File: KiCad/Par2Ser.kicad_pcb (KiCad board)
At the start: 2 copper layers, 47 x 50 mm, 42 parts, among them J1 DB25_Male, J2 Arduino UART header, J3 USB_C_Receptacle_USB2.0, J4 Conn_01x02, Q1 BC857, U1 Arduino_Nano_V3, U2 FT232RNL-REEL, U3 SC16IS750IBS,128, X1 Abracon-ASFL1-7.3728MHZ-EK-T

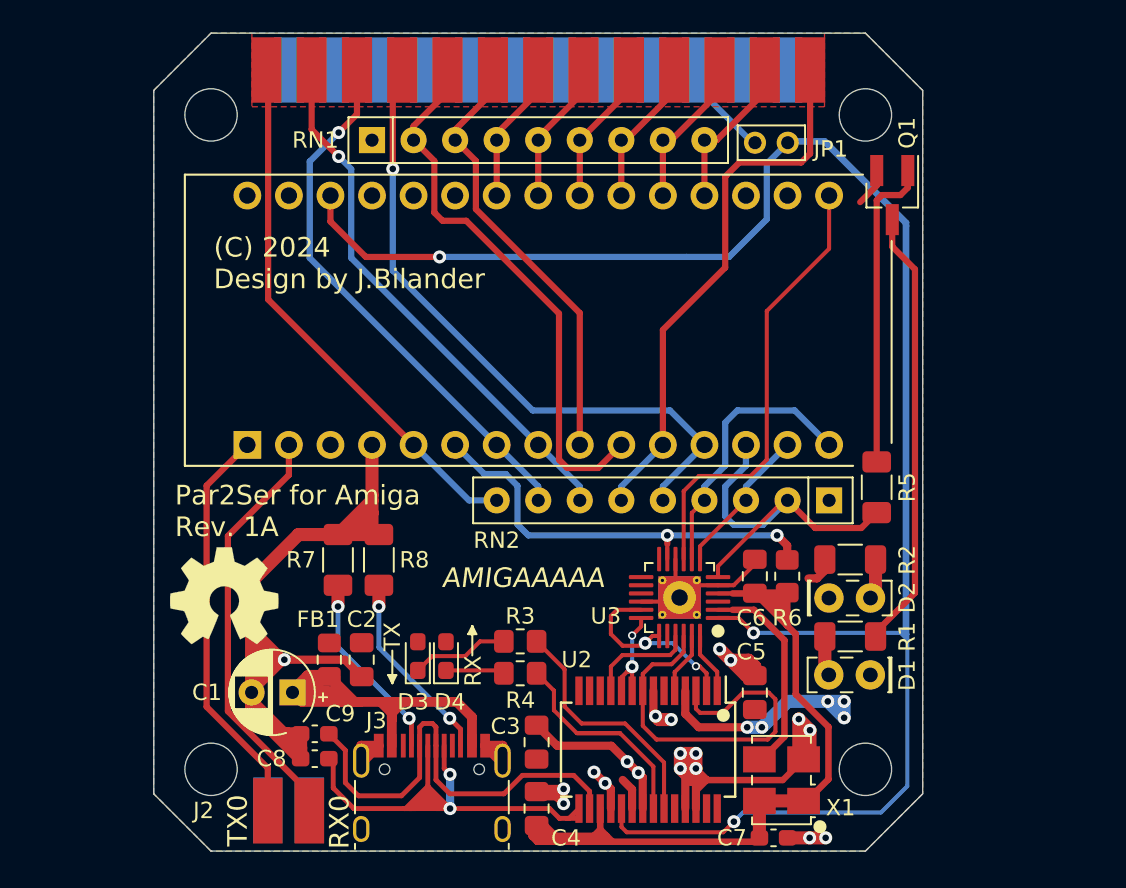
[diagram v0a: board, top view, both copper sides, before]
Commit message: Add LC4032V-5TN48C CPLD and remove Arduino Nano
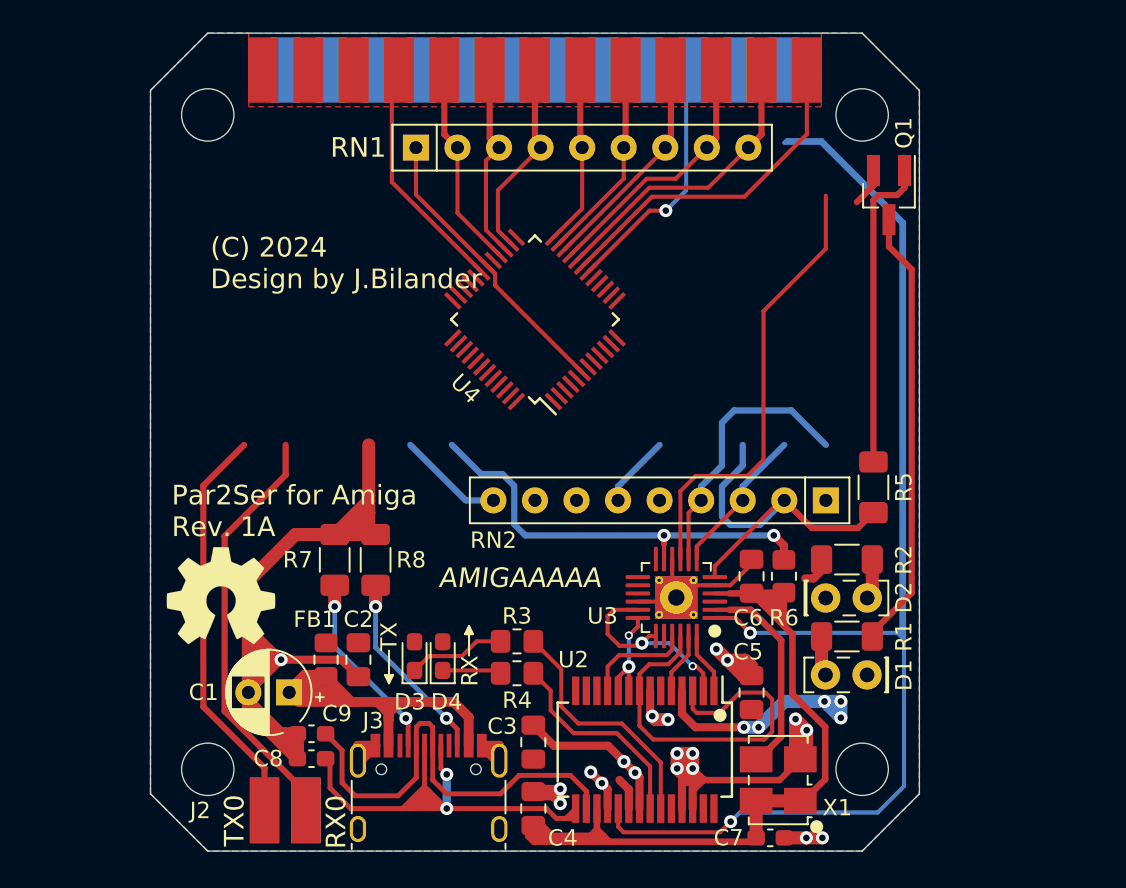
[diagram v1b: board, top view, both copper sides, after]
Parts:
- removed the ? at (128.6, 125.3)
- removed the ? at (134.8, 125.3)
- removed the ? at (163.3, 124.2)
- removed the ? at (169.6, 124.2)
- removed the ? at (163.3, 119.5)
- removed the ? at (169.7, 119.5)
- removed JP1: PinHeader for 2mm Shunt Jumper, Connector_PinHeader_2.00mm:PinHeader_1x02_P2.00mm_Vertical
- removed U1: Arduino_Nano_V3, Par2Ser:Arduino_Nano_V3
- added ?: , , B.Cu at (128.3, 125.3)
- added ?: , , B.Cu at (134.7, 125.3)
- added ?: , , B.Cu at (163.1, 124.2)
- added ?: , , B.Cu at (169.4, 124.2)
- added ?: , , B.Cu at (163.1, 119.5)
- added ?: , , B.Cu at (169.5, 119.5)
- added U4: LC4032V-5TN48C, Package_QFP:TQFP-48_7x7mm_P0.5mm, F.Cu at (147.5, 102.5)
- moved RN1 14.1 mm to (151.7, 92.0)
- moved C1 0.20 mm to (132.5, 125.3)
- moved C7 0.20 mm to (161.9, 134.2)
- moved D3 0.20 mm to (140.1, 123.1)
- moved FB1 0.20 mm to (134.7, 123.3)
- moved Q1 0.20 mm to (169.1, 94.9)
- moved R1 0.20 mm to (166.6, 121.9)
- moved R2 0.20 mm to (166.6, 117.2)
- moved R7 0.20 mm to (135.3, 117.2)
- moved R8 0.20 mm to (137.8, 117.2)
- moved U3 0.20 mm to (156.1, 119.5)
- moved C2 0.20 mm to (136.7, 123.3)
- moved C3 0.20 mm to (147.4, 128.3)
- moved C4 0.20 mm to (147.4, 132.4)
- moved C5 0.20 mm to (160.7, 125.3)
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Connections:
- J1 pad 16: Amiga_RESET -> RESET
- RN1 pad 1: VCC -> 3V3
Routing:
- net BUSY: track 33.3 -> 0.00 mm, vias 1 -> 0
- net POUT: track 33.1 -> 0.00 mm, vias 1 -> 0
- net SELECT: track 33.1 -> 6.48 mm
- net ACK: track 40.4 -> 14.8 mm, vias 1 -> 0
- net D7: track 33.8 -> 12.7 mm
- net RESET: track 146.1 -> 127.5 mm
- net 3V3: track 59.5 -> 77.5 mm
- net D6: track 27.0 -> 12.0 mm
- net D0: track 9.64 -> 18.4 mm
- net STROBE: track 33.3 -> 25.4 mm
- net Amiga_RESET: track 7.08 -> 0.00 mm
- net D1: track 9.41 -> 16.0 mm
- net D2: track 9.18 -> 13.6 mm
- net D5: track 8.73 -> 12.1 mm
- net D3: track 8.92 -> 12.3 mm
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
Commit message: Remove unused components and begin pin assigment on CPLD, place and route pull-up resistor networks and series resistor networks for parallel port signals
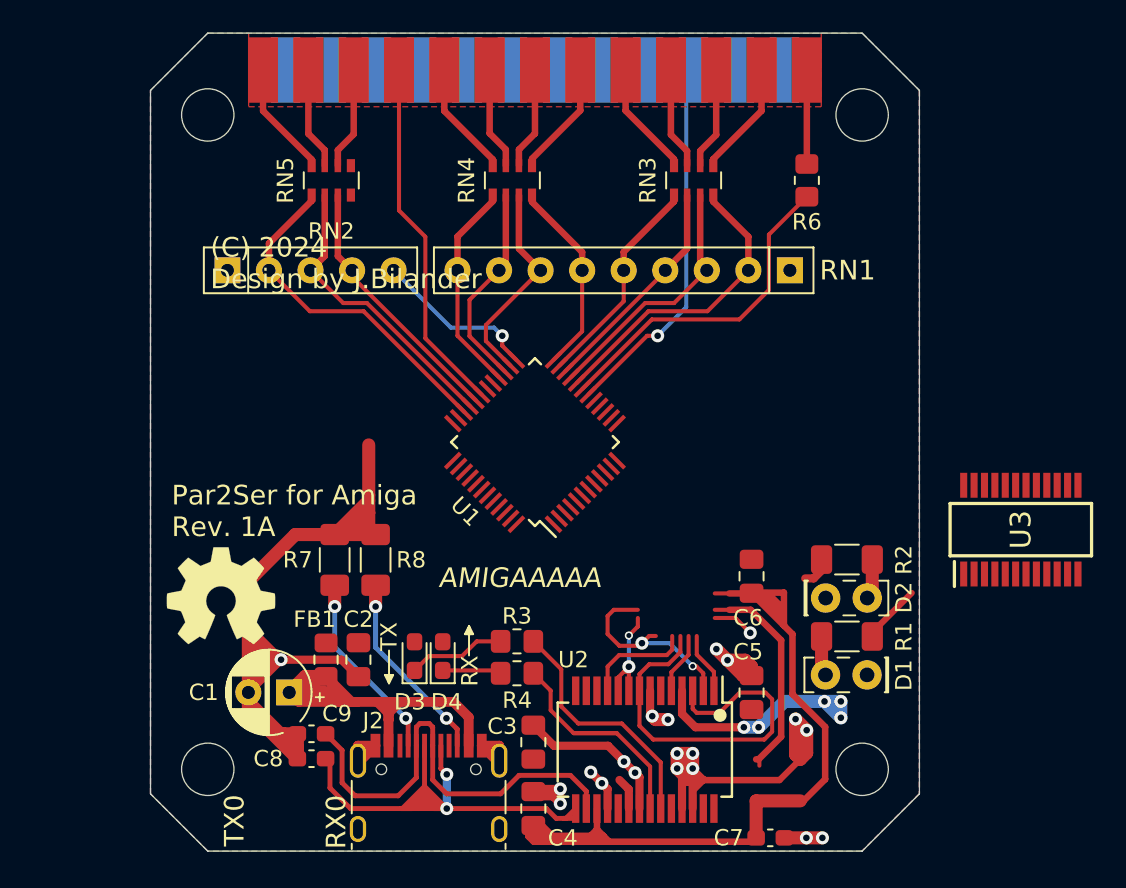
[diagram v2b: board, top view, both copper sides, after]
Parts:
- removed the J2 at (132.2, 132.6)
- removed J4: Conn_01x02, Par2Ser:PinSocket_1x02_P2.54mm_SMD
- removed Q1: BC857, Package_TO_SOT_SMD:SOT-23_Handsoldering
- removed R5: 4k7, Resistor_SMD:R_1206_3216Metric_Pad1.30x1.75mm_HandSolder
- removed X1: Abracon-ASFL1-7.3728MHZ-EK-T, Oscillator:Oscillator_SMD_SeikoEpson_SG8002LB-4Pin_5.0x3.2mm
- added RN3: 330, Resistor_SMD:R_Array_Convex_4x0603, F.Cu at (157.2, 94.0)
- added RN4: 330, Resistor_SMD:R_Array_Convex_4x0603, F.Cu at (146.1, 94.0)
- added RN5: 330, Resistor_SMD:R_Array_Convex_4x0603, F.Cu at (135.1, 94.0)
- R6: value 1k 0805 -> 330
- RN2: footprint Resistor_THT:R_Array_SIP9 -> Resistor_THT:R_Array_SIP5
- U3: value SC16IS750IBS,128 -> FT240XS-R; footprint Par2Ser:HVQFN-24-1EP_4x4mm_P0.5mm_EP2.6x2.6mm_HandSolder -> Par2Ser:SOP64P599X175-24N
- moved RN2 33.3 mm to (135.1, 99.5), turned to 0 degrees
- moved R6 24.2 mm to (164.1, 94.0)
- moved U3 21.5 mm to (177.2, 115.3), turned to 90 degrees
- moved RN1 7.50 mm to (151.7, 99.5), turned to 180 degrees
- moved U1 7.50 mm to (147.5, 110.0)
- renumbered J3 to J2, U4 to U1
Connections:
- net Net-(U4-Pad2) renamed D5_3V3
- net Net-(U4-Pad3) renamed D6_3V3
- net Net-(U4-Pad4) renamed D7_3V3
- net Net-(U4-Pad44) renamed D0_3V3
- net Net-(U4-Pad45) renamed D1_3V3
- net Net-(U4-Pad46) renamed D2_3V3
- net Net-(U4-Pad47) renamed D3_3V3
- net Net-(U4-Pad48) renamed D4_3V3
- net SCK renamed Net-(U3-Pad9)
- R1 pad 1: /Collector -> Net-(R1-Pad1)
- R2 pad 1: VCC -> 3V3
- R6 pad 1: IRQ -> STROBE
- R6 pad 2: 3V3 -> /STRB
- RN1 pad 2: D7 -> D0_B0
- RN1 pad 3: D6 -> D1_B1
- RN1 pad 4: D5 -> D2_B2
- RN1 pad 5: D4 -> D3_B3
- RN1 pad 6: D3 -> D4_B4
- RN1 pad 7: D2 -> D5_B5
- RN1 pad 8: D1 -> D6_B6
- RN1 pad 9: D0 -> D7_B7
- RN2 pad 1: VCC -> 3V3
- RN2 pad 2: SS -> SELECT_B11
- RN2 pad 3: MOSI -> POUT_B10
- RN2 pad 4: MISO -> BUSY_B9
- RN2 pad 5: ACK -> TMS
- U1 pad 12: 1V8 -> 3V3
- U1 pad 19: STROBE -> /STRB
- U1 pad 20: D0 -> D0_B0
- U1 pad 21: D1 -> D1_B1
- U1 pad 22: D2 -> D2_B2
- U1 pad 23: D3 -> D3_B3
- U1 pad 24: D4 -> D4_B4
- U1 pad 26: D5 -> D5_B5
- U1 pad 27: D6 -> D6_B6
- U1 pad 28: D7 -> D7_B7
- U1 pad 32: POUT -> BUSY_B9
- U1 pad 33: SELECT -> POUT_B10
- U1 pad 34: BUSY -> SELECT_B11
- U1 pad 36: 1V8 -> 3V3
- U3 pad 1: RESET -> Net-(U3-Pad1)
- U3 pad 10: GND -> Net-(U3-Pad10)
- U3 pad 11: IRQ -> Net-(U3-Pad11)
- U3 pad 16: GND -> Net-(U3-Pad16)
- U3 pad 17: DSR -> Net-(U3-Pad17)
- U3 pad 18: DTR -> Net-(U3-Pad18)
- U3 pad 19: DSR -> Net-(U3-Pad19)
- U3 pad 2: 7M -> Net-(U3-Pad2)
- U3 pad 21: RTS -> Net-(U3-Pad21)
- U3 pad 22: CTS -> Net-(U3-Pad22)
- U3 pad 23: TX -> Net-(U3-Pad23)
- U3 pad 24: RX -> Net-(U3-Pad24)
- U3 pad 4: 3V3 -> Net-(U3-Pad4)
- U3 pad 5: GND -> Net-(U3-Pad5)
- U3 pad 6: SS -> Net-(U3-Pad6)
- U3 pad 7: MOSI -> Net-(U3-Pad7)
- U3 pad 8: MISO -> Net-(U3-Pad8)
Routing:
- net RESET: track 127.5 -> 26.5 mm, vias 3 -> 2
- net Net-(U3-Pad9): track 27.8 -> 0.00 mm
- net /Collector: track 27.2 -> 0.00 mm
- net IRQ: track 27.0 -> 0.00 mm, vias 2 -> 0
- net RX0: track 26.0 -> 0.00 mm
- net TX0: track 25.0 -> 0.00 mm
- net SS: track 22.7 -> 0.00 mm
- net SELECT_B11: track 0.00 -> 21.2 mm
- net /STRB: track 0.00 -> 20.6 mm
- net STROBE: track 25.4 -> 5.75 mm
- net /Base: track 19.4 -> 0.00 mm
- net D0_B0: track 0.00 -> 18.8 mm
- net POUT_B10: track 0.00 -> 18.2 mm
- net MISO: track 16.7 -> 0.00 mm
- net 3V3: track 77.5 -> 61.4 mm
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
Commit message: Replace FT232RNL with FT240X and do some routing
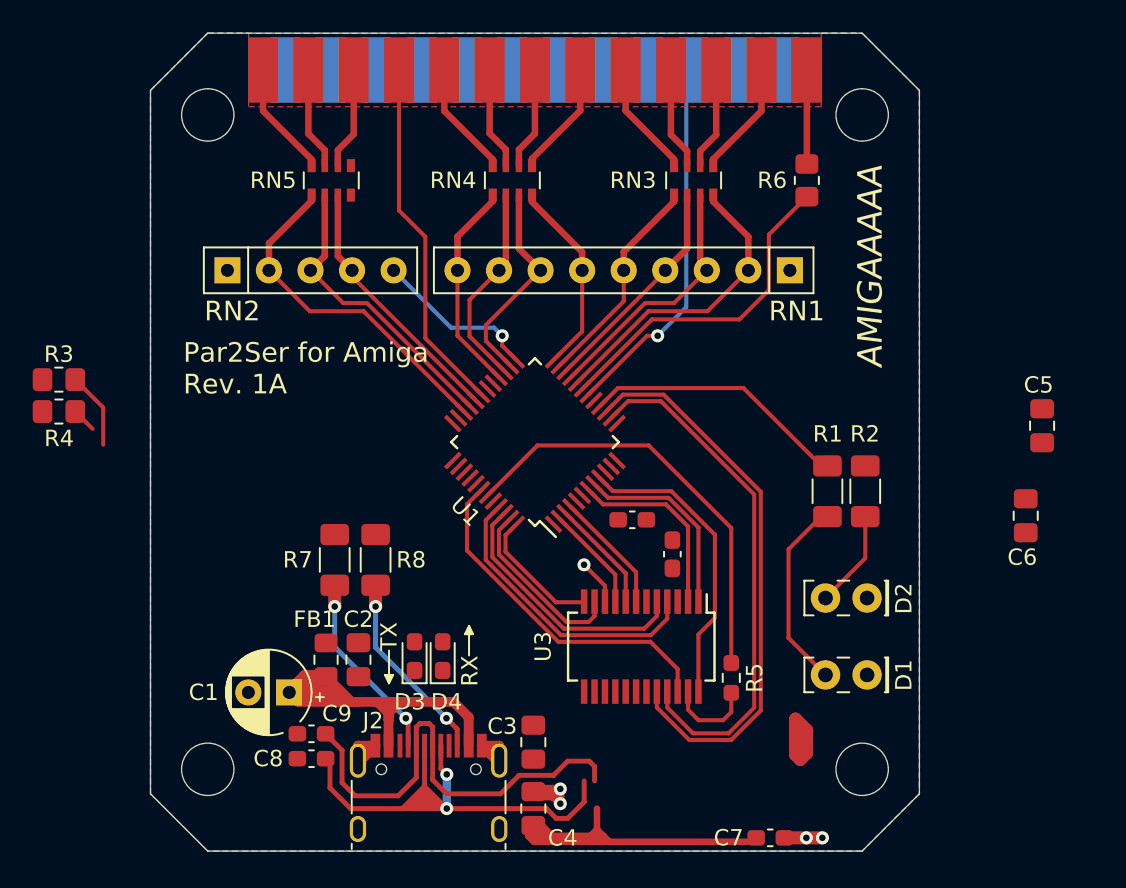
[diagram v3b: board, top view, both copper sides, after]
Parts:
- removed ? (x6): , 
- removed the REF** at (148.8, 102.5)
- removed the REF** at (128.3, 119.4)
- removed U2: FT232RNL-REEL, Package_SO:SSOP-28_5.3x10.2mm_P0.65mm
- added R5: 33, Resistor_SMD:R_0603_1608Metric_Pad0.98x0.95mm_HandSolder, F.Cu at (159.5, 124.4)
- added REF**: C_0603_1608Metric_Pad1.08x0.95mm_HandSolder, Capacitor_SMD:C_0603_1608Metric_Pad1.08x0.95mm_HandSolder, F.Cu at (153.4, 114.8)
- added REF**: C_0603_1608Metric_Pad1.08x0.95mm_HandSolder, Capacitor_SMD:C_0603_1608Metric_Pad1.08x0.95mm_HandSolder, F.Cu at (155.9, 116.8)
- U3: footprint Par2Ser:SOP64P599X175-24N -> Package_SO:SSOP-24_3.9x8.7mm_P0.635mm
- moved R3 32.2 mm to (118.4, 106.2)
- moved R4 32.2 mm to (118.4, 108.1)
- moved U3 24.3 mm to (154.0, 122.5), turned to 270 degrees
- moved C5 24.1 mm to (178.5, 109.0)
- moved C6 17.2 mm to (177.5, 114.5)
- moved R1 8.95 mm to (165.4, 113.0), turned to 270 degrees
- moved R2 4.32 mm to (167.7, 113.0), turned to 270 degrees
- moved D2 2.53 mm to (167.8, 119.5), turned to 180 degrees
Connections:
- net Net-(U3-Pad17) renamed /VCORE
- R1 pad 1: Net-(R1-Pad1) -> ACT_LED
- U1 pad 14: Net-(U1-Pad14) -> RXF
- U1 pad 15: Net-(U1-Pad15) -> TXE
- U1 pad 16: Net-(U1-Pad16) -> ACT_LED
- U1 pad 2: D5_3V3 -> D3_3V3
- U1 pad 4: D7_3V3 -> D5_3V3
- U1 pad 42: Net-(U1-Pad42) -> CBUS6
- U1 pad 43: Net-(U1-Pad43) -> CLK12M
- U1 pad 44: D0_3V3 -> Net-(U1-Pad44)
- U1 pad 46: D2_3V3 -> D7_3V3
- U1 pad 47: D3_3V3 -> RD
- U1 pad 48: D4_3V3 -> WR
- U1 pad 7: Net-(U1-Pad7) -> D2_3V3
- U1 pad 8: Net-(U1-Pad8) -> D4_3V3
- U1 pad 9: Net-(U1-Pad9) -> D0_3V3
- U3 pad 1: Net-(U3-Pad1) -> D4_3V3
- U3 pad 10: Net-(U3-Pad10) -> 3V3
- U3 pad 11: Net-(U3-Pad11) -> RD
- U3 pad 12: Net-(U3-Pad12) -> WR
- U3 pad 13: Net-(U3-Pad13) -> USBDP
- U3 pad 14: Net-(U3-Pad14) -> USBDM
- U3 pad 15: Net-(U3-Pad15) -> 3V3
- U3 pad 16: Net-(U3-Pad16) -> 3V3
- U3 pad 18: Net-(U3-Pad18) -> 3V3
- U3 pad 19: Net-(U3-Pad19) -> GND
- U3 pad 2: Net-(U3-Pad2) -> D2_3V3
- U3 pad 20: Net-(U3-Pad20) -> TXE
- U3 pad 21: Net-(U3-Pad21) -> RXF
- U3 pad 22: Net-(U3-Pad22) -> CBUS6
- U3 pad 23: Net-(U3-Pad23) -> /CLK12M_RAW
- U3 pad 24: Net-(U3-Pad24) -> D0_3V3
- U3 pad 3: Net-(U3-Pad3) -> 3V3
- U3 pad 4: Net-(U3-Pad4) -> D1_3V3
- U3 pad 5: Net-(U3-Pad5) -> D7_3V3
- U3 pad 6: Net-(U3-Pad6) -> GND
- U3 pad 7: Net-(U3-Pad7) -> D5_3V3
- U3 pad 8: Net-(U3-Pad8) -> D6_3V3
- U3 pad 9: Net-(U3-Pad9) -> D3_3V3
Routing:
- net GND: track 125.4 -> 19.2 mm, vias 19 -> 4
- net TXE: track 0.00 -> 34.7 mm
- net RXF: track 0.00 -> 32.2 mm
- net 3V3: track 61.4 -> 29.9 mm, vias 0 -> 1
- net CLK12M: track 0.00 -> 26.5 mm
- net CTS: track 24.6 -> 0.00 mm
- net CBUS6: track 0.00 -> 21.3 mm
- net D0_3V3: track 0.00 -> 18.4 mm
- net D1_3V3: track 0.00 -> 18.0 mm
- net VCC: track 16.5 -> 0.00 mm, vias 5 -> 0
- net D7_3V3: track 0.00 -> 16.1 mm
- net ACT_LED: track 0.00 -> 16.0 mm
- net RXLED: track 15.4 -> 1.50 mm
- net 7M: track 13.3 -> 0.00 mm
- net DSR: track 12.2 -> 0.00 mm, vias 2 -> 0
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- added copper zone on F.Cu, net GND
- removed copper zone on F.Cu, net VCC
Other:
- board text removed: "GND"
- board text removed: "RX0"
- board text removed: "TX0"

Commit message: Fix placement and routing of caps and resistors
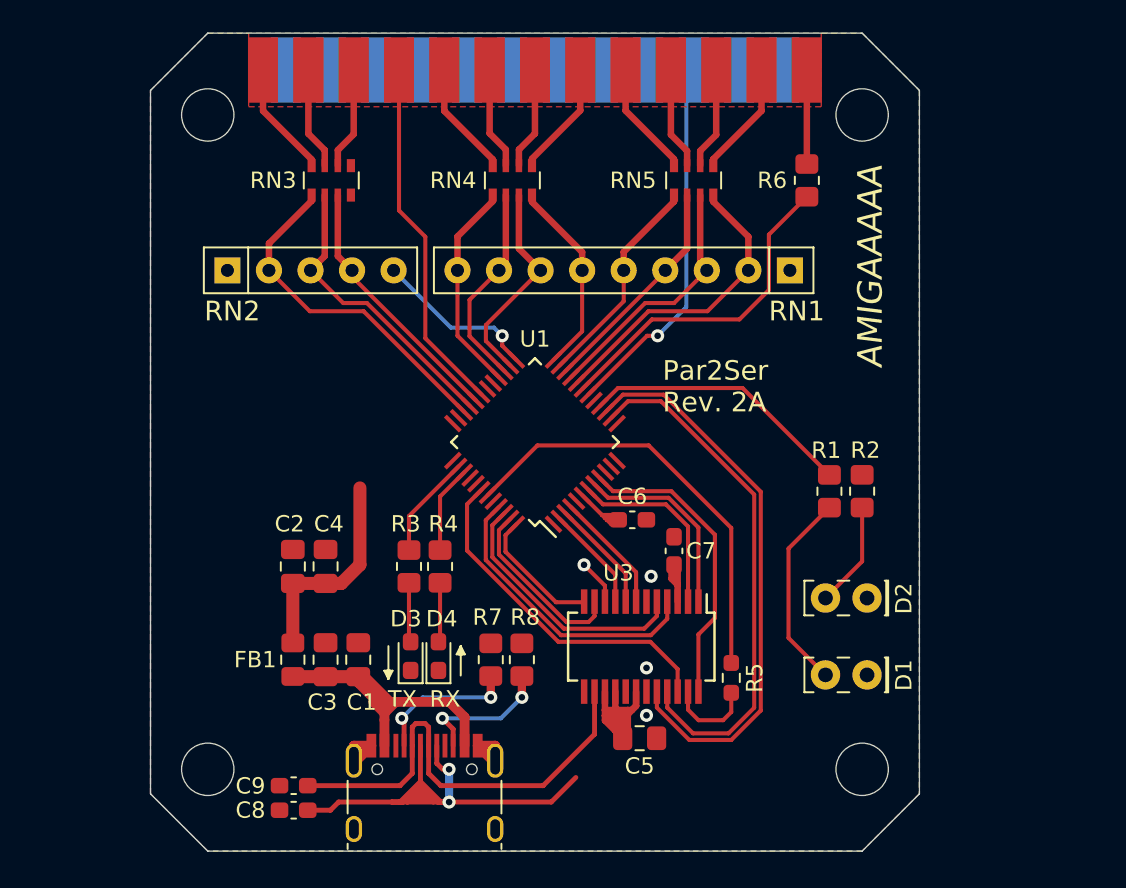
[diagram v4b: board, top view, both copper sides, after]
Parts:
- removed the C4 at (147.4, 132.4)
- removed REF** (x2): C_0603_1608Metric_Pad1.08x0.95mm_HandSolder, Capacitor_SMD:C_0603_1608Metric_Pad1.08x0.95mm_HandSolder
- added C3: 0.1uF, Capacitor_SMD:C_0805_2012Metric_Pad1.18x1.45mm_HandSolder, F.Cu at (134.7, 123.3)
- C1: value 100uF Radial Pitch_2.5mm -> 4.7uF; footprint Capacitor_THT:CP_Radial_D5.0mm_P2.50mm -> Capacitor_SMD:C_0805_2012Metric_Pad1.18x1.45mm_HandSolder
- C2: value 4.7uF (0805) -> 4.7uF
- C6: footprint Capacitor_SMD:C_0805_2012Metric_Pad1.18x1.45mm_HandSolder -> Capacitor_SMD:C_0603_1608Metric_Pad1.08x0.95mm_HandSolder
- R1, R2, R7, R8: footprint Resistor_SMD:R_1206_3216Metric_Pad1.30x1.75mm_HandSolder -> Resistor_SMD:R_0805_2012Metric_Pad1.20x1.40mm_HandSolder
- moved C4 44.6 mm to (134.7, 117.6)
- moved R4 25.2 mm to (141.7, 117.6), turned to 90 degrees
- moved R3 24.3 mm to (139.8, 117.6), turned to 90 degrees
- moved C6 24.1 mm to (153.4, 114.8), turned to 0 degrees
- moved C7 18.5 mm to (156.0, 116.7), turned to 270 degrees
- moved R7 11.3 mm to (144.8, 123.3)
- moved R8 10.8 mm to (146.7, 123.3)
- moved C2 6.97 mm to (132.7, 117.6), turned to 90 degrees
- moved C5 6.50 mm to (153.9, 128.1), turned to 0 degrees
- moved C1 4.67 mm to (136.7, 123.3), turned to 90 degrees
- moved C9 3.35 mm to (132.8, 131.0)
- moved C8 3.33 mm to (132.8, 132.5)
- moved FB1 2.03 mm to (132.7, 123.3)
- moved D4 0.26 mm to (141.6, 123.1)
- moved J2 0.25 mm to (140.8, 132.6)
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- renumbered C5 to C4, C3 to C5, RN5 to RN3, RN3 to RN5
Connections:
- C5 pad 1: VCC -> 3V3
- C7 pad 1: 3V3 -> GND
- C7 pad 2: GND -> 3V3
- D3 pad 1: Net-(D3-Pad1) -> GND
- D3 pad 2: VCC -> Net-(D3-Pad2)
- D4 pad 1: Net-(D4-Pad1) -> GND
- D4 pad 2: VCC -> Net-(D4-Pad2)
- R3 pad 1: TXLED -> Net-(D3-Pad2)
- R3 pad 2: Net-(D3-Pad1) -> TXLED
- R4 pad 1: RXLED -> Net-(D4-Pad2)
- R4 pad 2: Net-(D4-Pad1) -> RXLED
- U1 pad 38: Net-(U1-Pad38) -> TXLED
- U1 pad 39: Net-(U1-Pad39) -> RXLED
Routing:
- net VCC: track 0.00 -> 12.9 mm
- net GND: track 19.2 -> 6.87 mm, vias 4 -> 3
- net /VBUS: track 31.0 -> 20.2 mm
- net USBDP: track 41.1 -> 35.9 mm
- net RXLED: track 1.50 -> 5.38 mm
- net Net-(D4-Pad2): track 0.00 -> 3.65 mm
- net Net-(D3-Pad2): track 0.00 -> 3.65 mm
- net /CC2: track 11.9 -> 8.64 mm
- net /CC1: track 11.7 -> 9.00 mm
- net TXLED: track 4.69 -> 6.37 mm
- net 3V3: track 29.9 -> 31.0 mm
- net Net-(D1-Pad2): track 11.4 -> 12.2 mm
- net ACT_LED: track 16.0 -> 16.7 mm
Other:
- board text added: "Par2Ser Rev. 2A"
- board text removed: "Par2Ser for Amiga Rev. 1A"
